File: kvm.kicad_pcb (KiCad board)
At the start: 2 copper layers, 8 parts, among them J0 USB_C_Receptacle, J1 USB_C_Receptacle, J2 USB_C_Receptacle, U0 HD3SS3212, U1 HD3SS3212, U2 HD3SS3212

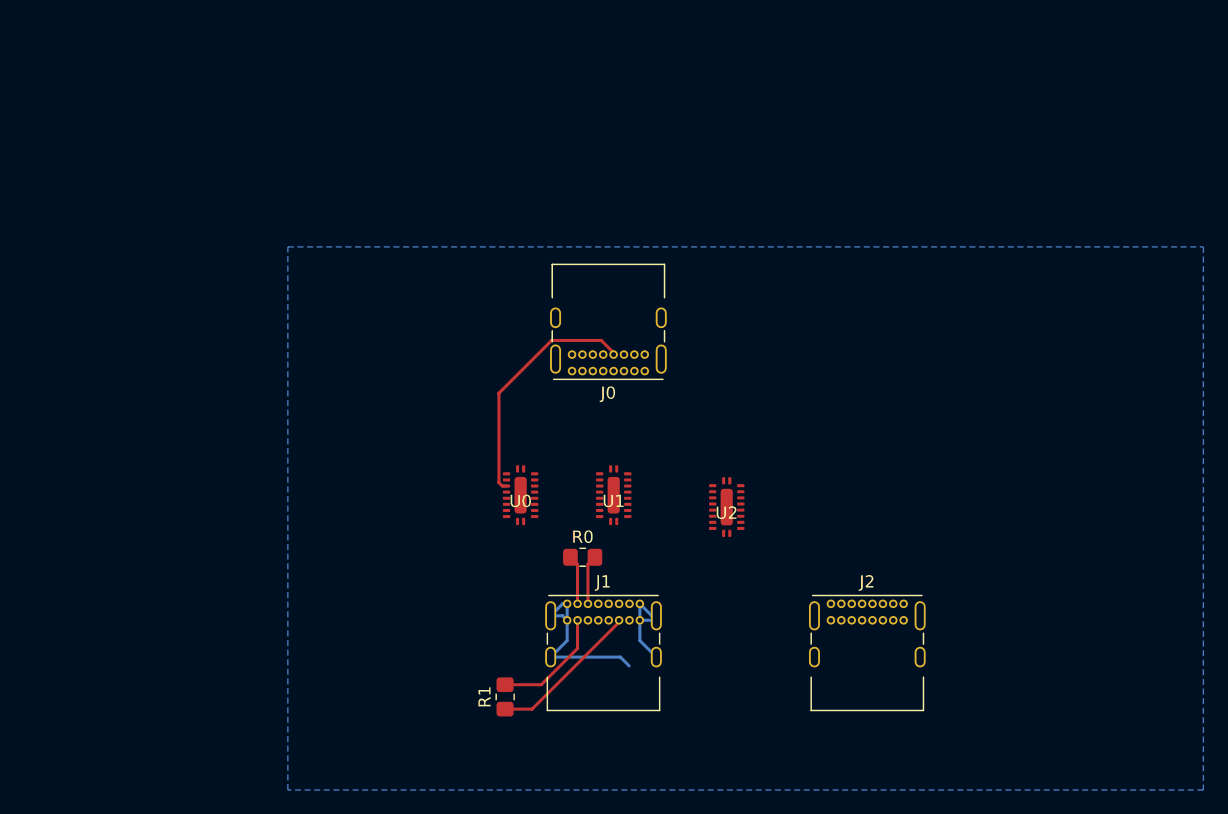
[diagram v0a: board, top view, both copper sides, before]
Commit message: Added a micro controller and SWD header
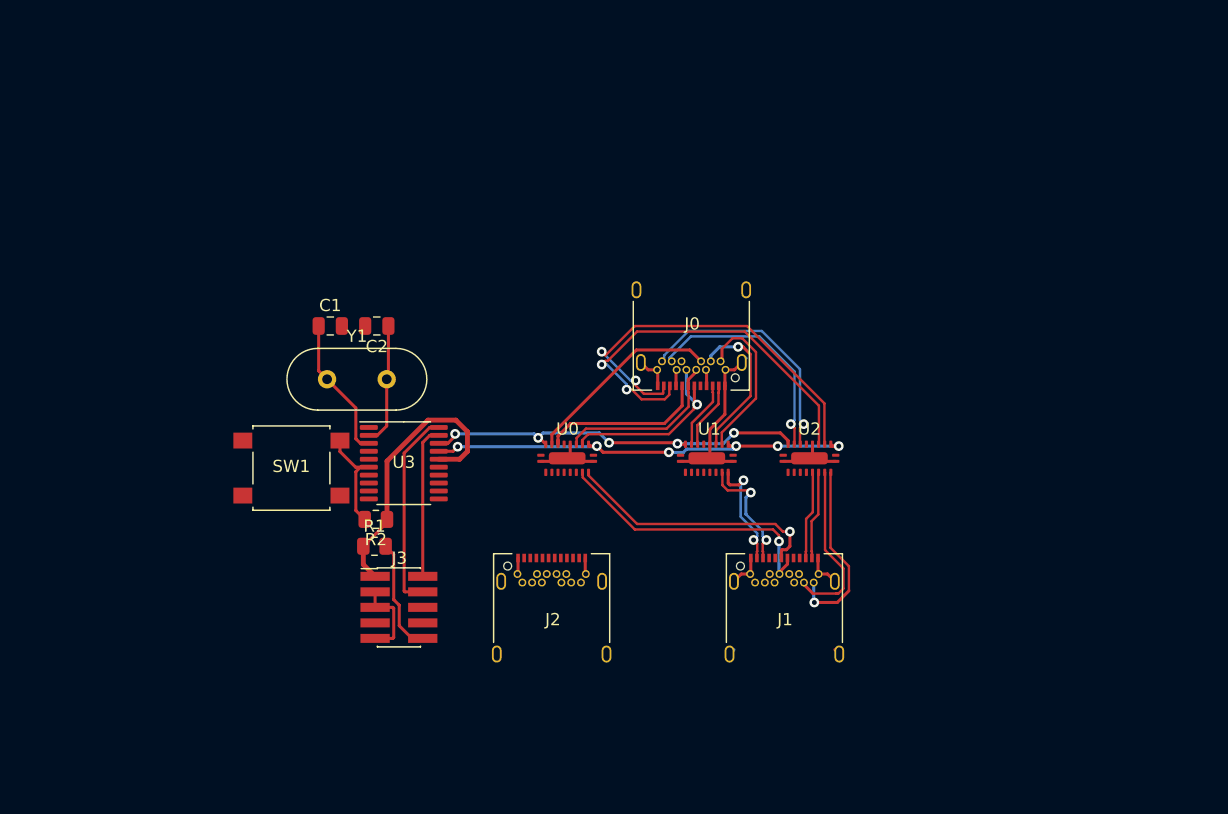
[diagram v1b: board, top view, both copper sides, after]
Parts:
- removed R0: 56k, Resistor_SMD:R_0805_2012Metric_Pad1.20x1.40mm_HandSolder
- added C1: 30p, Capacitor_SMD:C_0805_2012Metric, F.Cu at (70.8, 19.2)
- added C2: 30p, Capacitor_SMD:C_0805_2012Metric, F.Cu at (74.6, 19.2)
- added J3: Conn_ARM_JTAG_SWD_10, Connector_PinHeader_1.27mm:PinHeader_2x05_P1.27mm_Vertical_SMD, F.Cu at (76.4, 42.2)
- added R2: 10k, Resistor_SMD:R_0805_2012Metric, F.Cu at (74.5, 35.0)
- added SW1: SW_Push, Button_Switch_SMD:SW_SPST_B3S-1000, F.Cu at (67.6, 30.8)
- added U3: STM32F030F4Px, Package_SO:TSSOP-20_4.4x6.5mm_P0.65mm, F.Cu at (76.8, 30.4)
- added Y1: Crystal, Crystal:Crystal_HC49-4H_Vertical, F.Cu at (70.5, 23.5)
- J0, J1, J2: footprint Connector_USB:USB_C_Receptacle_GCT_USB4085 -> Connector_USB:USB_C_Receptacle_Amphenol_12401548E4-2A
- R1: value 56k -> 10k; footprint Resistor_SMD:R_0805_2012Metric_Pad1.20x1.40mm_HandSolder -> Resistor_SMD:R_0805_2012Metric
- moved J2 22.9 mm to (88.9, 43.2)
- moved J1 17.8 mm to (108.0, 43.2)
- moved R1 16.3 mm to (74.4, 37.2), turned to 0 degrees
- moved U1 8.20 mm to (101.6, 30.0), turned to 270 degrees
- moved U2 7.86 mm to (110.0, 30.0), turned to 270 degrees
- moved J0 5.39 mm to (100.3, 19.1)
- moved U0 4.86 mm to (90.2, 30.0), turned to 270 degrees
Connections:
- J0 pad A5: Net-(J0-PadA5) -> (no net)
- J0 pad A6: Net-(J0-PadA6) -> /OD+
- J0 pad A7: Net-(J0-PadA7) -> /OD-
- J0 pad A8: Net-(J0-PadA8) -> /OSBU1
- J0 pad B5: Net-(J0-PadB5) -> (no net)
- J0 pad B6: Net-(J0-PadB6) -> /OD+
- J0 pad B7: Net-(J0-PadB7) -> /OD-
- J0 pad B8: Net-(J0-PadB8) -> /OSBU2
- J1 pad A5: Net-(J1-PadA5) -> (no net)
- J1 pad A6: Net-(J1-PadA6) -> /I1D+
- J1 pad A7: Net-(J1-PadA7) -> /I1D-
- J1 pad A8: Net-(J1-PadA8) -> /I1SBU1
- J1 pad B5: Net-(J1-PadB5) -> (no net)
- J1 pad B6: Net-(J1-PadB6) -> /I1D+
- J1 pad B7: Net-(J1-PadB7) -> /I1D-
- J1 pad B8: Net-(J1-PadB8) -> /I1SBU2
- J2 pad A4: Net-(J0-PadA4) -> Net-(J2-PadA4)
- J2 pad A5: Net-(J0-PadA5) -> (no net)
- J2 pad A6: Net-(J2-PadA6) -> /I2D+
- J2 pad A7: Net-(J2-PadA7) -> /I2D-
- J2 pad A8: Net-(J0-PadA8) -> /I2SBU1
- J2 pad A9: Net-(J0-PadA4) -> Net-(J2-PadA4)
- J2 pad B4: Net-(J0-PadA4) -> Net-(J2-PadA4)
- J2 pad B5: Net-(J0-PadB5) -> (no net)
- J2 pad B6: Net-(J2-PadB6) -> /I2D+
- J2 pad B7: Net-(J2-PadB7) -> /I2D-
- J2 pad B8: Net-(J0-PadB8) -> /I2SBU2
- J2 pad B9: Net-(J0-PadA4) -> Net-(J2-PadA4)
- R1 pad 1: Net-(J1-PadB5) -> +3V3
- R1 pad 2: Net-(J1-PadA4) -> /NRST
- U0 pad 1: Net-(U0-Pad1) -> (no net)
- U0 pad 10: Net-(U0-Pad10) -> (no net)
- U0 pad 12: Net-(J1-PadA7) -> /I2SBU2
- U0 pad 13: Net-(J1-PadB6) -> /I2SBU1
- U0 pad 14: Net-(J1-PadB7) -> /I2D-
- U0 pad 15: Net-(J1-PadA6) -> /I2D+
- U0 pad 16: Net-(U0-Pad16) -> /I1SBU2
- U0 pad 17: Net-(U0-Pad17) -> /I1SBU1
- U0 pad 18: Net-(U0-Pad18) -> /I1D-
- U0 pad 19: Net-(U0-Pad19) -> /I1D+
- U0 pad 3: Net-(J0-PadA6) -> /OD+
- U0 pad 4: Net-(J0-PadB7) -> /OD-
- U0 pad 7: Net-(J0-PadB6) -> /OSBU1
- U0 pad 8: Net-(J0-PadA7) -> /OSBU2
- U1 pad 1: Net-(U1-Pad1) -> (no net)
- U1 pad 10: Net-(U1-Pad10) -> (no net)
- U1 pad 12: Net-(J1-PadA3) -> /I2RX1-
- U1 pad 13: Net-(J1-PadA2) -> /I2RX1+
- U1 pad 14: Net-(J1-PadB10) -> /I2TX1-
- U1 pad 15: Net-(J1-PadB11) -> /I2TX1+
- U1 pad 16: Net-(J2-PadA3) -> /I1RX1-
- U1 pad 17: Net-(J2-PadA2) -> /I1RX1+
- U1 pad 18: Net-(J2-PadB10) -> /I1TX1-
- U1 pad 19: Net-(J2-PadB11) -> /I1TX1+
- U1 pad 3: Net-(J0-PadB11) -> /ORX1+
- U1 pad 4: Net-(J0-PadB10) -> /ORX1-
- U1 pad 7: Net-(J0-PadA2) -> /OTX1+
- U1 pad 8: Net-(J0-PadA3) -> /OTX1-
- U2 pad 1: Net-(U2-Pad1) -> (no net)
- U2 pad 10: Net-(U2-Pad10) -> (no net)
- U2 pad 12: Net-(J1-PadB3) -> /I2RX2-
- U2 pad 13: Net-(J1-PadB2) -> /I2RX2+
- U2 pad 14: Net-(J1-PadA10) -> /I2TX2-
- U2 pad 15: Net-(J1-PadA11) -> /I2TX2+
- U2 pad 16: Net-(J2-PadB3) -> /I1RX2-
- U2 pad 17: Net-(J2-PadB2) -> /I1RX2+
- U2 pad 18: Net-(J2-PadA10) -> /I1TX2-
- U2 pad 19: Net-(J2-PadA11) -> /I1TX2+
- U2 pad 3: Net-(J0-PadA11) -> /ORX2+
- U2 pad 4: Net-(J0-PadA10) -> /ORX2-
- U2 pad 7: Net-(J0-PadB2) -> /OTX2+
- U2 pad 8: Net-(J0-PadB3) -> /OTX2-
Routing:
- net /OE: track 0.00 -> 35.5 mm, vias 0 -> 6
- net /ORX2+: track 0.00 -> 32.7 mm, vias 0 -> 2
- net /ORX2-: track 0.00 -> 32.4 mm, vias 0 -> 2
- net /SEL: track 0.00 -> 32.1 mm, vias 0 -> 5
- net +3V3: track 0.00 -> 23.2 mm
- net /I1D-: track 0.00 -> 23.2 mm, vias 0 -> 1
- net GND: track 23.1 -> 45.2 mm
- net /I1D+: track 0.00 -> 21.3 mm, vias 0 -> 1
- net /OTX2+: track 0.00 -> 20.2 mm, vias 0 -> 1
- net Net-(J0-PadB7): track 19.8 -> 0.00 mm
- net /OTX2-: track 0.00 -> 18.7 mm, vias 0 -> 1
- net /SWCLK: track 0.00 -> 16.5 mm
- net /OSBU2: track 0.00 -> 16.3 mm
- net /OD+: track 0.00 -> 15.9 mm, vias 0 -> 1
- net /I1TX2+: track 0.00 -> 15.2 mm, vias 0 -> 1
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- removed copper zone on B.Cu, net GND

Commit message: finished PD switches and added 3.3V PSU
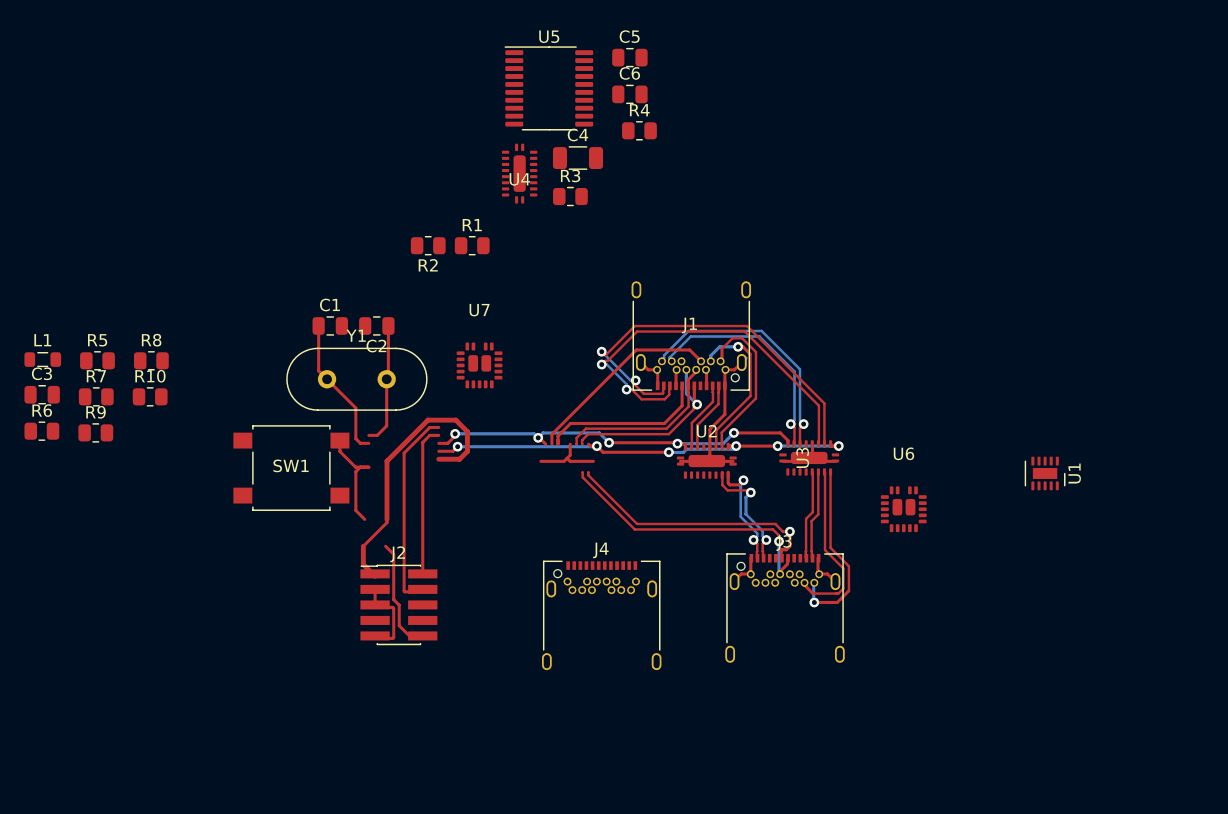
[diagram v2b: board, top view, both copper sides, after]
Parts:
- removed J0: USB_C_Receptacle, Connector_USB:USB_C_Receptacle_Amphenol_12401548E4-2A
- removed U0: HD3SS3212, VQFN20:VQFN20RKS
- added C3: 1u, Capacitor_SMD:C_0805_2012Metric, F.Cu at (47.2, 24.8)
- added C4: 10u, Capacitor_SMD:C_1206_3216Metric, F.Cu at (91.1, 5.43)
- added C5: 30p, Capacitor_SMD:C_0805_2012Metric, F.Cu at (95.3, -2.79)
- added C6: 30p, Capacitor_SMD:C_0805_2012Metric, F.Cu at (95.3, 0.22)
- added J4: USB_C_Receptacle, Connector_USB:USB_C_Receptacle_Amphenol_12401548E4-2A, F.Cu at (93.0, 43.8)
- added L1: 33u, Inductor_SMD:L_0805_2012Metric, F.Cu at (47.2, 21.9)
- added R10: 10k, Resistor_SMD:R_0805_2012Metric, F.Cu at (56.0, 25.0)
- added R3: 10k, Resistor_SMD:R_0805_2012Metric, F.Cu at (90.4, 8.58)
- added R4: 10k, Resistor_SMD:R_0805_2012Metric, F.Cu at (96.1, 3.20)
- added R5: 10k, Resistor_SMD:R_0805_2012Metric, F.Cu at (51.7, 22.0)
- added R6: 640, Resistor_SMD:R_0805_2012Metric, F.Cu at (47.2, 27.8)
- added R7: 10k, Resistor_SMD:R_0805_2012Metric, F.Cu at (51.6, 25.0)
- added R8: 640, Resistor_SMD:R_0805_2012Metric, F.Cu at (56.1, 22.0)
- added R9: 10k, Resistor_SMD:R_0805_2012Metric, F.Cu at (51.6, 27.9)
- added U4: HD3SS3212, VQFN20:VQFN20RKS, F.Cu at (86.3, 6.70)
- added U5: STM32F030F4Px, Package_SO:TSSOP-20_4.4x6.5mm_P0.65mm, F.Cu at (88.7, -0.27)
- added U6: UCS3205, VQFN20:VQFN19_3x3x0.9mm, F.Cu at (117.7, 34.2)
- added U7: UCS3205, VQFN20:VQFN19_3x3x0.9mm, F.Cu at (83.0, 22.4)
- C1: value 30p -> 1u
- C2: value 30p -> 3300p
- J2: value USB_C_Receptacle -> Conn_ARM_JTAG_SWD_10; footprint Connector_USB:USB_C_Receptacle_Amphenol_12401548E4-2A -> Connector_PinHeader_1.27mm:PinHeader_2x05_P1.27mm_Vertical_SMD
- J3: value Conn_ARM_JTAG_SWD_10 -> USB_C_Receptacle; footprint Connector_PinHeader_1.27mm:PinHeader_2x05_P1.27mm_Vertical_SMD -> Connector_USB:USB_C_Receptacle_Amphenol_12401548E4-2A
- R1: value 10k -> 3.32M
- R2: value 10k -> 866k
- U1: value HD3SS3212 -> MAX17501AxTB; footprint VQFN20:VQFN20RKS -> Package_DFN_QFN:TDFN-10-1EP_2x3mm_P0.5mm_EP0.9x2mm
- U3: value STM32F030F4Px -> HD3SS3212; footprint Package_SO:TSSOP-20_4.4x6.5mm_P0.65mm -> VQFN20:VQFN20RKS
- moved U3 33.2 mm to (110.0, 30.0), turned to 270 degrees
- moved J3 31.6 mm to (108.0, 43.2)
- moved U1 27.7 mm to (129.3, 31.2)
- moved R1 25.9 mm to (82.4, 12.6)
- moved J1 25.3 mm to (100.3, 19.1), turned to 180 degrees
- moved R2 22.8 mm to (78.8, 12.6)
- moved J2 12.6 mm to (76.4, 42.0)
- moved U2 8.40 mm to (101.6, 30.2)
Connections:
- C1 pad 1: /CRY1 -> VBUS
- C2 pad 1: /CRY0 -> Net-(C2-Pad1)
- J1 pad A10: /I1RX2- -> /ORX2-
- J1 pad A11: /I1RX2+ -> /ORX2+
- J1 pad A2: /I1TX1+ -> /OTX1+
- J1 pad A3: /I1TX1- -> /OTX1-
- J1 pad A4: Net-(J1-PadA4) -> VBUS
- J1 pad A6: /I1D+ -> /OD+
- J1 pad A7: /I1D- -> /OD-
- J1 pad A8: /I1SBU1 -> /OSBU1
- J1 pad A9: Net-(J1-PadA4) -> VBUS
- J1 pad B10: /I1RX1- -> /ORX1-
- J1 pad B11: /I1RX1+ -> /ORX1+
- J1 pad B2: /I1TX2+ -> /OTX2+
- J1 pad B3: /I1TX2- -> /OTX2-
- J1 pad B4: Net-(J1-PadA4) -> VBUS
- J1 pad B6: /I1D+ -> /OD+
- J1 pad B7: /I1D- -> /OD-
- J1 pad B8: /I1SBU2 -> /OSBU2
- J1 pad B9: Net-(J1-PadA4) -> VBUS
- R1 pad 1: +3V3 -> VBUS
- R1 pad 2: /NRST -> Net-(R1-Pad2)
- R2 pad 1: +3V3 -> Net-(R1-Pad2)
- R2 pad 2: Net-(R2-Pad2) -> GND
- SW1 pad 1: Net-(R2-Pad2) -> Net-(R4-Pad2)
- U1 pad 1: (no net) -> GND
- U1 pad 10: (no net) -> Net-(L1-Pad1)
- U1 pad 2: /OE -> VBUS
- U1 pad 3: /ORX1+ -> Net-(R1-Pad2)
- U1 pad 4: /ORX1- -> Net-(C3-Pad1)
- U1 pad 5: GND -> +3V3
- U1 pad 6: +3V3 -> Net-(C2-Pad1)
- U1 pad 7: /OTX1+ -> (no net)
- U1 pad 8: /OTX1- -> (no net)
- U1 pad 9: /SEL -> GND
- U2 pad 12: /I2RX2- -> /I2SBU2
- U2 pad 13: /I2RX2+ -> /I2SBU1
- U2 pad 14: /I2TX2- -> /I2D-
- U2 pad 15: /I2TX2+ -> /I2D+
- U2 pad 16: /I1RX2- -> /I1SBU2
- U2 pad 17: /I1RX2+ -> /I1SBU1
- U2 pad 18: /I1TX2- -> /I1D-
- U2 pad 19: /I1TX2+ -> /I1D+
- U2 pad 3: /ORX2+ -> /OD+
- U2 pad 4: /ORX2- -> /OD-
- U2 pad 7: /OTX2+ -> /OSBU1
- U2 pad 8: /OTX2- -> /OSBU2
- U3 pad 11: (no net) -> GND
- U3 pad 12: (no net) -> /I2RX1-
- U3 pad 13: (no net) -> /I2RX1+
- U3 pad 14: (no net) -> /I2TX1-
- U3 pad 15: GND -> /I2TX1+
- U3 pad 16: +3V3 -> /I1RX1-
- U3 pad 17: /OE -> /I1RX1+
- U3 pad 18: /SEL -> /I1TX1-
- U3 pad 19: /SWDIO -> /I1TX1+
- U3 pad 2: /CRY0 -> /OE
- U3 pad 20: /SWCLK -> GND
- U3 pad 3: /CRY1 -> /ORX1+
- U3 pad 4: /NRST -> /ORX1-
- U3 pad 5: (no net) -> GND
- U3 pad 6: Net-(R2-Pad2) -> +3V3
- U3 pad 7: (no net) -> /OTX1+
- U3 pad 8: (no net) -> /OTX1-
- U3 pad 9: (no net) -> /SEL
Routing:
- net /ORX2+: track 32.7 -> 0.00 mm, vias 2 -> 0
- net /ORX2-: track 32.4 -> 0.00 mm, vias 2 -> 0
- net /OTX2+: track 20.2 -> 0.00 mm, vias 1 -> 0
- net /ORX1-: track 12.8 -> 32.4 mm, vias 1 -> 2
- net /ORX1+: track 13.4 -> 32.7 mm, vias 0 -> 2
- net /OTX2-: track 18.7 -> 0.00 mm, vias 1 -> 0
- net /OTX1+: track 5.52 -> 20.2 mm, vias 0 -> 1
- net /OD+: track 15.9 -> 29.3 mm
- net /OTX1-: track 5.52 -> 18.7 mm, vias 0 -> 1
- net /OD-: track 14.0 -> 26.8 mm, vias 0 -> 1
- net Net-(R4-Pad2): track 0.00 -> 9.21 mm
- net Net-(R2-Pad2): track 9.21 -> 0.00 mm
- net /OSBU2: track 16.3 -> 21.8 mm
- net /OSBU1: track 13.8 -> 19.4 mm
- net GND: track 45.2 -> 41.5 mm
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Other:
- copper layers 2 -> 4
